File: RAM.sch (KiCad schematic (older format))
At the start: 14 parts, among them U35 74HC00, U36 74LS245, U37 74HC04, U38 74LS173, U39 74LS173, U40 74LS245, U41 74LS173, U42 74LS173, U43 AS6C6264, U44 AS6C6264, U45 AT28C64B-15PU, U46 AT28C64B-15PU

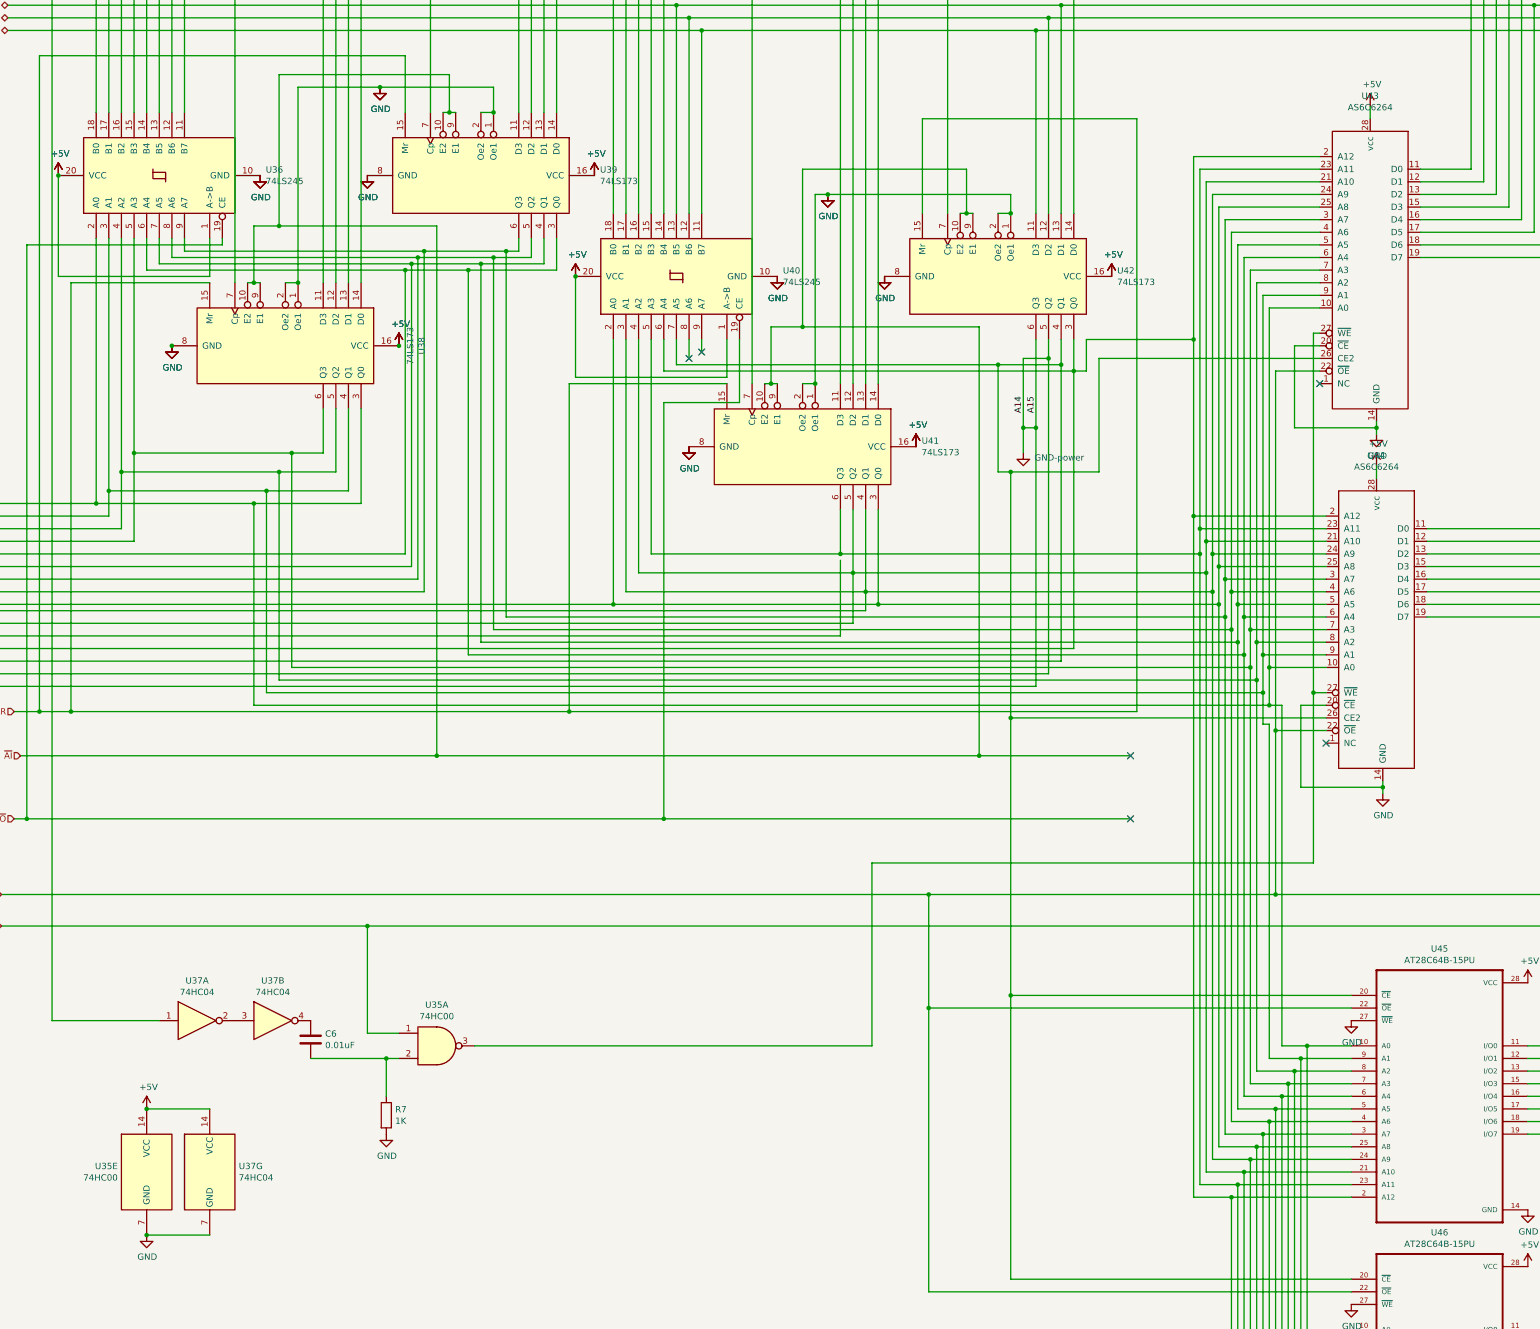
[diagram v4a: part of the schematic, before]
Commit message: Added NAND GATES in ALU
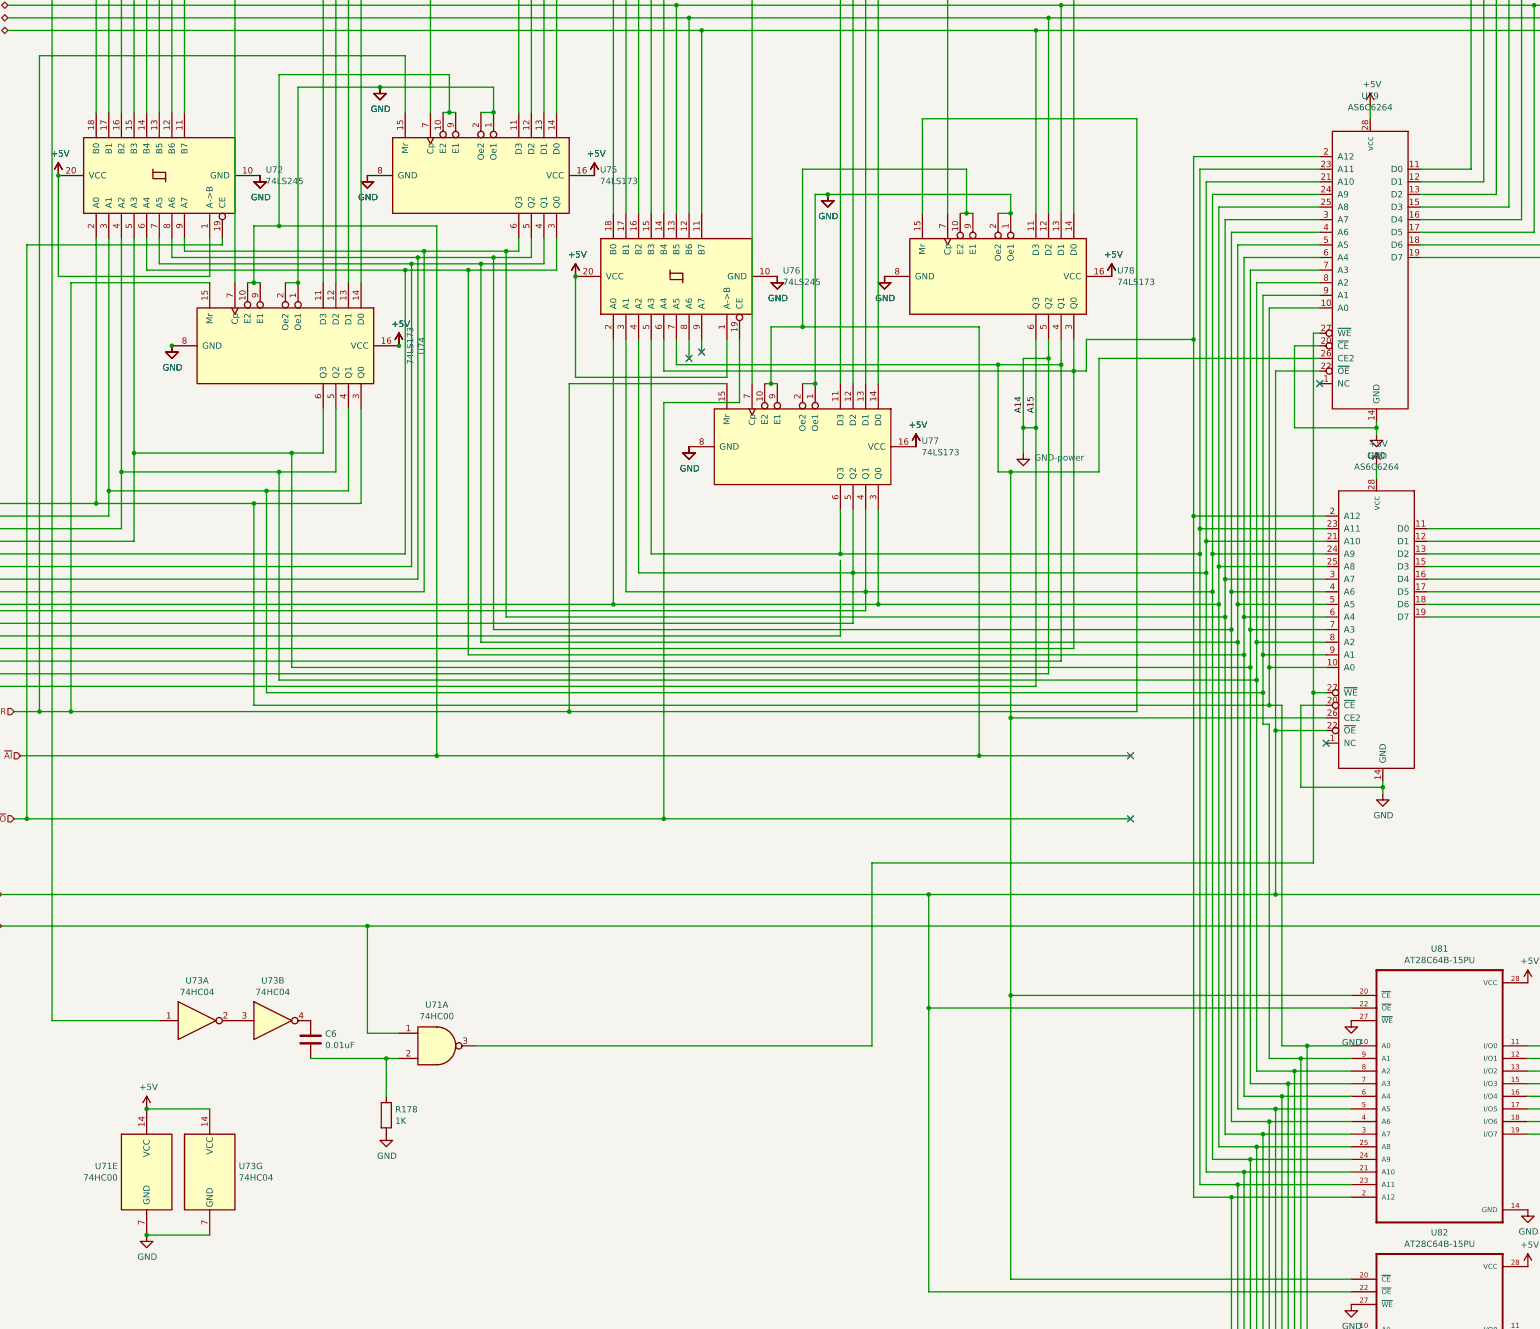
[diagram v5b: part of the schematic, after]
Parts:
- renumbered R7 to R178, U35 to U71, U36 to U72, U37 to U73, U38 to U74, U39 to U75, U40 to U76, U41 to U77, U42 to U78, U43 to U79, U44 to U80, U45 to U81, U46 to U82

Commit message: using new RAM and ROM,15bits baby
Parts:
- removed C6: 0.01uF, Capacitor_THT:CP_Axial_L10.0mm_D4.5mm_P15.00mm_Horizontal, symbol 16bitCpu-rescue:C-Device
- removed R178: 1K, Resistor_THT:R_Axial_DIN0204_L3.6mm_D1.6mm_P7.62mm_Horizontal, symbol 16bitCpu-rescue:R-Device
- removed U79, U80: AS6C6264, Package_DIP:DIP-28_W15.24mm, symbol draguve:AS6C6264
- removed U81, U82: AT28C64B-15PU, ROM:ZIF-AT28C64B-15PU, symbol AT28C64B-15PU:AT28C64B-15PU
- added U80, U81: AT28C256, ROM:ZIF-AT28C64B-15PU, symbol AT28C256:AT28C256
- added U82, U83: AS6C62256A, Package_DIP:DIP-28_W15.24mm, symbol draguve:AS6C62256A
- added U84: 74HC04, Package_DIP:DIP-14_W7.62mm, symbol 16bitCpu-rescue:74HC04-74xx
- renumbered U74 to U73, U75 to U74, U76 to U75, U77 to U76, U78 to U77, U73 to U78, U71 to U79
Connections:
- net +5V: now also U80.28 (VCC), U81.28 (VCC), U82.28 (VCC), U83.28 (VCC)
- net Bus0: now also U80.11 (IO0), U82.11 (IO0)
- net Bus1: now also U80.12 (IO1), U82.12 (IO1)
- net Bus10: now also U81.13 (IO2), U83.13 (IO2)
- net Bus11: now also U81.15 (IO3), U83.15 (IO3)
- net Bus12: now also U81.16 (IO4), U83.16 (IO4)
- net Bus13: now also U81.17 (IO5), U83.17 (IO5)
- net Bus14: now also U81.18 (IO6), U83.18 (IO6)
- net Bus15: now also U81.19 (IO7), U83.19 (IO7)
- net Bus2: now also U80.13 (IO2), U82.13 (IO2)
- net Bus3: now also U80.15 (IO3), U82.15 (IO3)
- net Bus4: now also U80.16 (IO4), U82.16 (IO4)
- net Bus5: now also U80.17 (IO5), U82.17 (IO5)
- net Bus6: now also U80.18 (IO6), U82.18 (IO6)
- net Bus7: now also U80.19 (IO7), U82.19 (IO7)
- net Bus8: now also U81.11 (IO0), U83.11 (IO0)
- net Bus9: now also U81.12 (IO1), U83.12 (IO1)
- net GND: now also U80.14 (GND), U81.14 (GND), U82.14 (GND), U83.14 (GND); no longer U77.5 (Q2), U77.6 (Q3)
- net sheet61B5B12C/I0: now also U80.10 (A0), U81.10 (A0), U82.10 (A0), U83.10 (A0)
- net sheet61B5B12C/I1: now also U80.9 (A1), U81.9 (A1), U82.9 (A1), U83.9 (A1)
- net sheet61B5B12C/I10: now also U80.21 (A10), U81.21 (A10), U82.21 (A10), U83.21 (A10)
- net sheet61B5B12C/I11: now also U75.5 (A3), U76.6 (Q3), U80.23 (A11), U81.23 (A11), U82.23 (A11), U83.23 (A11)
- net sheet61B5B12C/I12: now also U80.2 (A12), U81.2 (A12), U82.2 (A12), U83.2 (A12)
- net sheet61B5B12C/I13: now also U80.26 (A13), U81.26 (A13), U82.26 (A13), U83.26 (A13)
- net sheet61B5B12C/I2: now also U80.8 (A2), U81.8 (A2), U82.8 (A2), U83.8 (A2)
- net sheet61B5B12C/I3: now also U80.7 (A3), U81.7 (A3), U82.7 (A3), U83.7 (A3)
- net sheet61B5B12C/I4: now also U80.6 (A4), U81.6 (A4), U82.6 (A4), U83.6 (A4)
- net sheet61B5B12C/I5: now also U80.5 (A5), U81.5 (A5), U82.5 (A5), U83.5 (A5)
- net sheet61B5B12C/I6: now also U80.4 (A6), U81.4 (A6), U82.4 (A6), U83.4 (A6)
- net sheet61B5B12C/I7: now also U80.3 (A7), U81.3 (A7), U82.3 (A7), U83.3 (A7)
- net sheet61B5B12C/I8: now also U80.25 (A8), U81.25 (A8), U82.25 (A8), U83.25 (A8)
- net sheet61B5B12C/I9: now also U80.24 (A9), U81.24 (A9), U82.24 (A9), U83.24 (A9)
- net sheet61B5B12C/I14: now reaches U75.8 (A6)
- net sheet61B5B12C/I14: now also U77.5 (Q2), U80.1 (A14), U81.1 (A14), U82.1 (A14), U83.1 (A14)
- net sheet61B5B12C/I15: now reaches U75.9 (A7)
- net sheet61B5B12C/I15: now also U77.6 (Q3), U80.20 (~CE~), U81.20 (~CE~), U84.1
- net at U79.3: now also U82.27 (~WE~), U83.27 (~WE~)
- net at U79.2: now also U78.4
- new net: U80.22 (~OE~), U81.22 (~OE~), U82.22 (~OE~), U83.22 (~OE~)
- new net: U82.20 (~CE~), U83.20 (~CE~), U84.2
- no-connect marks 22 -> 20
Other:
- moved on the sheet: U78A, U78B, U78G, U79A, U79E

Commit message: using new ROM in CU and more jumps
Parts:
- renumbered U72 to U71, U73 to U72, U74 to U73, U75 to U74, U76 to U75, U77 to U76, U78 to U77, U79 to U78, U80 to U79, U81 to U80, U82 to U81, U83 to U82, U84 to U83
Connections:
- net ~MEMOE: now also U79.22 (~OE~), U80.22 (~OE~), U81.22 (~OE~), U82.22 (~OE~)
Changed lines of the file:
@@
 AR Path="/603B766D/5F6DE9AB" Ref="U?"  Part="1"
 AR Path="/5F74778C/5F6DE9AB" Ref="U?"  Part="1"
-AR Path="/5F681977/5F6DE9AB" Ref="U73"  Part="1"
-F 0 "U73" H 3550 5981 50  0000 C CNN
+AR Path="/5F681977/5F6DE9AB" Ref="U72"  Part="1"
+F 0 "U72" H 3550 5981 50  0000 C CNN
 F 1 "74LS173" H 3550 5890 50  0000 C CNN
 F 2 "Package_DIP:DIP-16_W7.62mm" H 3550 4900 50  0001 C CNN
@@
 AR Path="/603B766D/5F6DE9B1" Ref="U?"  Part="1"
 AR Path="/5F74778C/5F6DE9B1" Ref="U?"  Part="1"
-AR Path="/5F681977/5F6DE9B1" Ref="U72"  Part="1"
-F 0 "U72" V 2596 2706 50  0000 R CNN
+AR Path="/5F681977/5F6DE9B1" Ref="U71"  Part="1"
+F 0 "U71" V 2596 2706 50  0000 R CNN
 F 1 "74LS245" V 2505 2706 50  0000 R CNN
 F 2 "Package_DIP:DIP-20_W7.62mm" H 2550 3550 50  0001 C CNN
@@
 AR Path="/603B766D/5F6DE9B7" Ref="U?"  Part="1"
 AR Path="/5F74778C/5F6DE9B7" Ref="U?"  Part="1"
-AR Path="/5F681977/5F6DE9B7" Ref="U77"  Part="1"
-F 0 "U77" V 9154 5294 50  0000 L CNN
+AR Path="/5F681977/5F6DE9B7" Ref="U76"  Part="1"
+F 0 "U76" V 9154 5294 50  0000 L CNN
 F 1 "74LS173" V 9245 5294 50  0000 L CNN
 F 2 "Package_DIP:DIP-16_W7.62mm" H 9200 4350 50  0001 C CNN
@@
 AR Path="/603B766D/5F6DEA26" Ref="U?"  Part="1"
 AR Path="/5F74778C/5F6DEA26" Ref="U?"  Part="1"
-AR Path="/5F681977/5F6DEA26" Ref="U76"  Part="1"
-F 0 "U76" V 7604 6644 50  0000 L CNN
+AR Path="/5F681977/5F6DEA26" Ref="U75"  Part="1"
+F 0 "U75" V 7604 6644 50  0000 L CNN
 F 1 "74LS173" V 7695 6644 50  0000 L CNN
 F 2 "Package_DIP:DIP-16_W7.62mm" H 7650 5700 50  0001 C CNN
@@
 AR Path="/603B766D/5F6DEA2C" Ref="U?"  Part="1"
 AR Path="/5F74778C/5F6DEA2C" Ref="U?"  Part="1"
-AR Path="/5F681977/5F6DEA2C" Ref="U74"  Part="1"
-F 0 "U74" V 5054 4494 50  0000 L CNN
+AR Path="/5F681977/5F6DEA2C" Ref="U73"  Part="1"
+F 0 "U73" V 5054 4494 50  0000 L CNN
 F 1 "74LS173" V 5145 4494 50  0000 L CNN
 F 2 "Package_DIP:DIP-16_W7.62mm" H 5100 3550 50  0001 C CNN
@@
 AR Path="/603B766D/5F6DEA34" Ref="U?"  Part="1"
 AR Path="/5F74778C/5F6DEA34" Ref="U?"  Part="1"
-AR Path="/5F681977/5F6DEA34" Ref="U75"  Part="1"
-F 0 "U75" V 6696 3506 50  0000 R CNN
+AR Path="/5F681977/5F6DEA34" Ref="U74"  Part="1"
+F 0 "U74" V 6696 3506 50  0000 R CNN
 F 1 "74LS245" V 6605 3506 50  0000 R CNN
 F 2 "Package_DIP:DIP-20_W7.62mm" H 6650 4350 50  0001 C CNN
@@
 P 12850 14100
 AR Path="/60C0C0E9" Ref="U?"  Part="1"
-AR Path="/5F681977/60C0C0E9" Ref="U79"  Part="1"
-F 0 "U79" H 12850 14425 50  0000 C CNN
+AR Path="/5F681977/60C0C0E9" Ref="U78"  Part="1"
+F 0 "U78" H 12850 14425 50  0000 C CNN
 F 1 "74HC00" H 12850 14334 50  0000 C CNN
 F 2 "Package_DIP:DIP-14_W7.62mm" H 12850 14100 50  0001 C CNN
@@
 P 10950 14200
 AR Path="/6116F1B1" Ref="U?"  Part="1"
-AR Path="/5F681977/6116F1B1" Ref="U78"  Part="1"
-F 0 "U78" H 10950 14517 50  0000 C CNN
+AR Path="/5F681977/6116F1B1" Ref="U77"  Part="1"
+F 0 "U77" H 10950 14517 50  0000 C CNN
 F 1 "74HC04" H 10950 14426 50  0000 C CNN
 F 2 "Package_DIP:DIP-14_W7.62mm" H 10950 14200 50  0001 C CNN
@@
 P 11550 14200
 AR Path="/61170EAC" Ref="U?"  Part="2"
-AR Path="/5F681977/61170EAC" Ref="U78"  Part="2"
-F 0 "U78" H 11550 14517 50  0000 C CNN
+AR Path="/5F681977/61170EAC" Ref="U77"  Part="2"
+F 0 "U77" H 11550 14517 50  0000 C CNN
 F 1 "74HC04" H 11550 14426 50  0000 C CNN
 F 2 "Package_DIP:DIP-14_W7.62mm" H 11550 14200 50  0001 C CNN
@@
 P 20550 13700
 AR Path="/609104EF" Ref="U?"  Part="7"
-AR Path="/5F681977/609104EF" Ref="U78"  Part="7"
-F 0 "U78" H 20780 13746 50  0000 L CNN
+AR Path="/5F681977/609104EF" Ref="U77"  Part="7"
+F 0 "U77" H 20780 13746 50  0000 L CNN
 F 1 "74HC04" H 20780 13655 50  0000 L CNN
 F 2 "Package_DIP:DIP-14_W7.62mm" H 20550 13700 50  0001 C CNN
@@
 P 20050 13700
 AR Path="/609949CC" Ref="U?"  Part="5"
-AR Path="/5F681977/609949CC" Ref="U79"  Part="5"
-F 0 "U79" H 19821 13746 50  0000 R CNN
+AR Path="/5F681977/609949CC" Ref="U78"  Part="5"
+F 0 "U78" H 19821 13746 50  0000 R CNN
 F 1 "74HC00" H 19821 13655 50  0000 R CNN
 F 2 "Package_DIP:DIP-14_W7.62mm" H 20050 13700 50  0001 C CNN
@@
 $EndComp
 $Comp
-L AT28C256:AT28C256 U80
+L AT28C256:AT28C256 U79
 U 1 1 604040AC
 P 13900 5800
-F 0 "U80" H 13900 6867 50  0000 C CNN
+F 0 "U79" H 13900 6867 50  0000 C CNN
 F 1 "AT28C256" H 13900 6776 50  0000 C CNN
 F 2 "ROM:ZIF-AT28C64B-15PU" H 13900 5800 50  0001 C CNN
@@
 	14500 5800 15450 5800
 $Comp
-L AT28C256:AT28C256 U81
+L AT28C256:AT28C256 U80
 U 1 1 609CE542
 P 13900 7650
-F 0 "U81" H 13900 8717 50  0000 C CNN
+F 0 "U80" H 13900 8717 50  0000 C CNN
 F 1 "AT28C256" H 13900 8626 50  0000 C CNN
 F 2 "ROM:ZIF-AT28C64B-15PU" H 13900 7650 50  0001 C CNN
@@
 	12200 10500 12200 8250
 $Comp
-L draguve:AS6C62256A U82
+L draguve:AS6C62256A U81
 U 1 1 60D34B50
 P 13900 8900
-F 0 "U82" H 13900 8967 50  0000 C CNN
+F 0 "U81" H 13900 8967 50  0000 C CNN
 F 1 "AS6C62256A" H 13900 8876 50  0000 C CNN
 F 2 "Package_DIP:DIP-28_W15.24mm" H 13900 8900 50  0001 C CNN
@@
 	16250 12550 14500 12550
 $Comp
-L draguve:AS6C62256A U83
+L draguve:AS6C62256A U82
 U 1 1 60EFF0C3
 P 13900 10950
-F 0 "U83" H 13900 11017 50  0000 C CNN
+F 0 "U82" H 13900 11017 50  0000 C CNN
 F 1 "AS6C62256A" H 13900 10926 50  0000 C CNN
 F 2 "Package_DIP:DIP-28_W15.24mm" H 13900 10950 50  0001 C CNN
@@
 $EndComp
 Wire Wire Line
-	1550 10700 16250 10700
-Wire Wire Line
 	12250 10600 12250 8650
 Wire Wire Line
@@
 P 15000 9000
 AR Path="/61770F6F" Ref="U?"  Part="1"
-AR Path="/5F681977/61770F6F" Ref="U84"  Part="1"
-F 0 "U84" H 15000 9317 50  0000 C CNN
+AR Path="/5F681977/61770F6F" Ref="U83"  Part="1"
+F 0 "U83" H 15000 9317 50  0000 C CNN
 F 1 "74HC04" H 15000 9226 50  0000 C CNN
 F 2 "Package_DIP:DIP-14_W7.62mm" H 15000 9000 50  0001 C CNN
@@
 Wire Wire Line
 	1000 650  1000 14200
+Wire Wire Line
+	1500 10700 16250 10700
 $EndSCHEMATC
